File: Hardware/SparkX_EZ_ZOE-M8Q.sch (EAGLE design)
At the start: 41 parts, among them J4 U.FL, Q2 20V/4.2A/52mΩ/1.4W, U1 UBLOX_ZOE_M8-0-10, X1 32.768kHz

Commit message: Review updates
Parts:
- U1: value UBLOX_ZOE_M8-0-10 -> U-BLOX_ZOE_M8Q-0-10; device SparkFun-GPS:UBLOX_ZOE_M8-0-10 -> SparkFun-GPS:U-BLOX_ZOE_M8Q-0-10
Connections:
- net V_BATT renamed PROC_PWR_EN
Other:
- moved on the sheet: C10, C11, L1, RXD, TXD, X1, ~{SAFEBOOT}

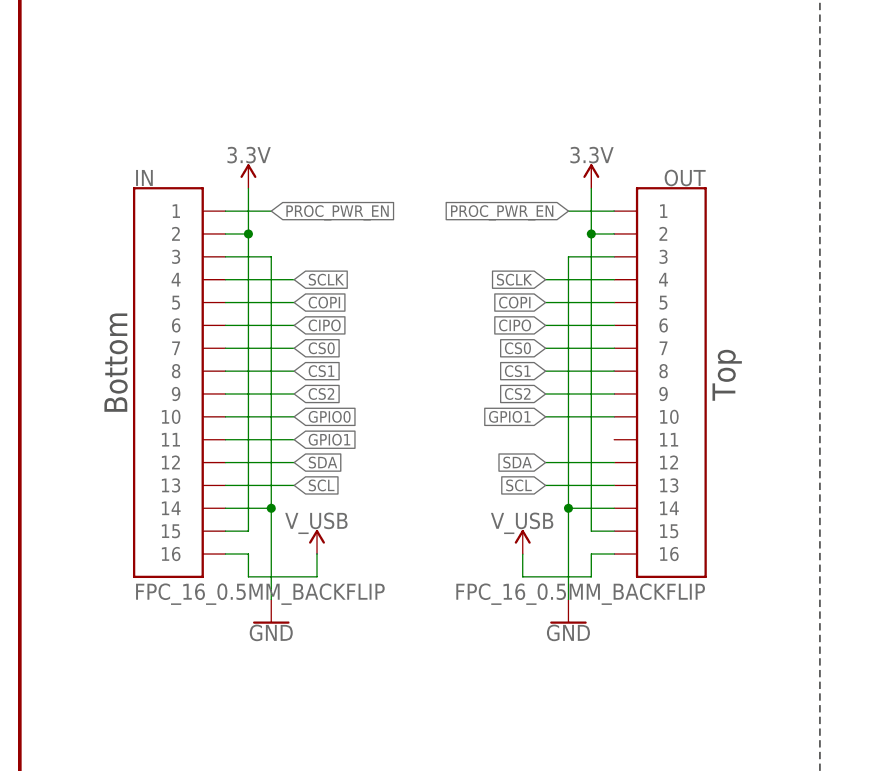
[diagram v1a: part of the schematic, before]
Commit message: Update 16-way FPC Connector
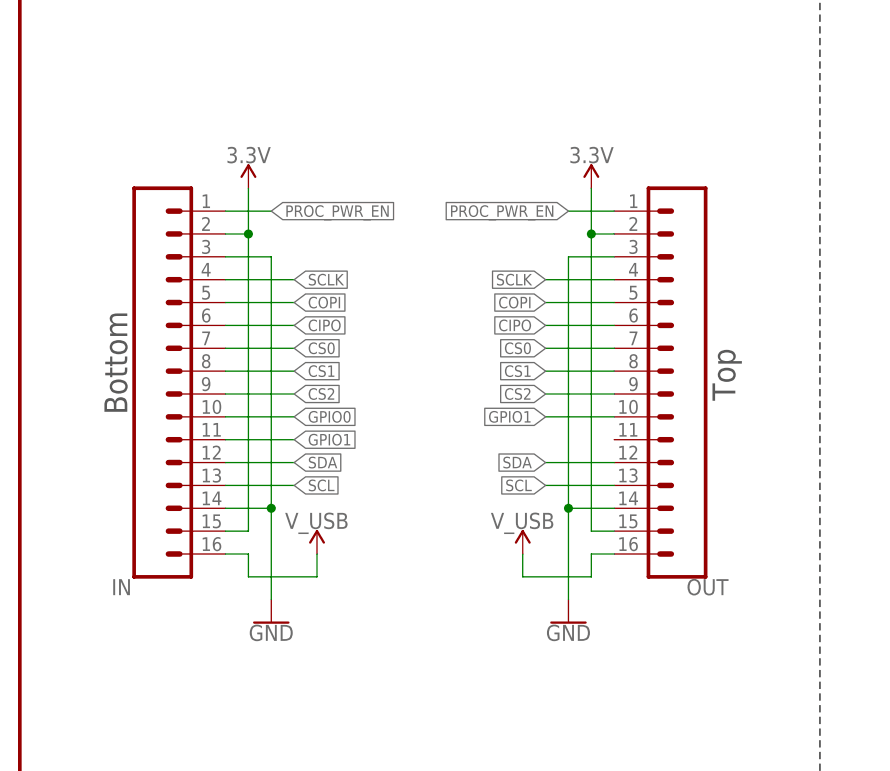
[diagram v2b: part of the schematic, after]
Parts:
- IN, OUT: value FPC_16_0.5MM_BACKFLIP -> (none); device New_Parts_Connectors:FPC_16_0.5MM_BACKFLIP -> SparkFun-Connectors:CONN_16FPC_16_0.5MM
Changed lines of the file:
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@@
 <part name="GND14" library="SparkFun-PowerSymbols" deviceset="GND" device=""/>
 <part name="SUPPLY4" library="SparkFun-PowerSymbols" deviceset="VDD" device=""/>
-<part name="IN" library="New_Parts_Connectors" deviceset="FPC_16_0.5MM" device="_BACKFLIP"/>
-<part name="OUT" library="New_Parts_Connectors" deviceset="FPC_16_0.5MM" device="_BACKFLIP"/>
+<part name="IN" library="SparkFun-Connectors" deviceset="CONN_16" device="FPC_16_0.5MM"/>
+<part name="OUT" library="SparkFun-Connectors" deviceset="CONN_16" device="FPC_16_0.5MM"/>
 <part name="SUPPLY21" library="SparkFun-PowerSymbols" deviceset="3.3V" device=""/>
 <part name="SUPPLY22" library="SparkFun-PowerSymbols" deviceset="3.3V" device=""/>
@@
 <instance part="LOGO3" gate="G$1" x="307.34" y="25.4" smashed="yes"/>
 <instance part="U$4" gate="G$1" x="307.34" y="7.62" smashed="yes"/>
-<instance part="IN" gate="G$1" x="15.24" y="45.72" smashed="yes">
-<attribute name="NAME" x="12.7" y="66.294" size="1.778" layer="95"/>
-<attribute name="VALUE" x="12.7" y="20.32" size="1.778" layer="96"/>
-</instance>
-<instance part="OUT" gate="G$1" x="73.66" y="45.72" smashed="yes" rot="MR0">
-<attribute name="NAME" x="76.2" y="66.294" size="1.778" layer="95" rot="MR0"/>
-<attribute name="VALUE" x="76.2" y="20.32" size="1.778" layer="96" rot="MR0"/>
+<instance part="IN" gate="G$1" x="12.7" y="43.18" smashed="yes" rot="MR180">
+<attribute name="NAME" x="10.16" y="22.606" size="1.778" layer="95" rot="MR180"/>
+<attribute name="VALUE" x="10.16" y="68.58" size="1.778" layer="96" rot="MR180"/>
+</instance>
+<instance part="OUT" gate="G$1" x="76.2" y="43.18" smashed="yes" rot="R180">
+<attribute name="NAME" x="78.74" y="22.606" size="1.778" layer="95" rot="R180"/>
+<attribute name="VALUE" x="78.74" y="68.58" size="1.778" layer="96" rot="R180"/>
 </instance>
 <instance part="SUPPLY21" gate="G$1" x="25.4" y="66.04" smashed="yes">
@@
 <segment>
 <pinref part="SUPPLY21" gate="G$1" pin="3.3V"/>
-<wire x1="25.4" y1="66.04" x2="25.4" y2="60.96" width="0.1524" layer="91"/>
 <pinref part="IN" gate="G$1" pin="2"/>
-<wire x1="25.4" y1="60.96" x2="22.86" y2="60.96" width="0.1524" layer="91"/>
 <pinref part="IN" gate="G$1" pin="15"/>
 <wire x1="22.86" y1="27.94" x2="25.4" y2="27.94" width="0.1524" layer="91"/>
 <wire x1="25.4" y1="27.94" x2="25.4" y2="60.96" width="0.1524" layer="91"/>
+<wire x1="25.4" y1="60.96" x2="25.4" y2="66.04" width="0.1524" layer="91"/>
+<wire x1="22.86" y1="60.96" x2="25.4" y2="60.96" width="0.1524" layer="91"/>
 <junction x="25.4" y="60.96"/>
 </segment>
 <segment>
 <pinref part="SUPPLY22" gate="G$1" pin="3.3V"/>
-<wire x1="63.5" y1="66.04" x2="63.5" y2="60.96" width="0.1524" layer="91"/>
 <pinref part="OUT" gate="G$1" pin="2"/>
-<wire x1="63.5" y1="60.96" x2="66.04" y2="60.96" width="0.1524" layer="91"/>
 <pinref part="OUT" gate="G$1" pin="15"/>
 <wire x1="66.04" y1="27.94" x2="63.5" y2="27.94" width="0.1524" layer="91"/>
 <wire x1="63.5" y1="27.94" x2="63.5" y2="60.96" width="0.1524" layer="91"/>
+<wire x1="63.5" y1="60.96" x2="63.5" y2="66.04" width="0.1524" layer="91"/>
+<wire x1="66.04" y1="60.96" x2="63.5" y2="60.96" width="0.1524" layer="91"/>
 <junction x="63.5" y="60.96"/>
 </segment>
@@
 <pinref part="IN" gate="G$1" pin="16"/>
 <wire x1="22.86" y1="25.4" x2="25.4" y2="25.4" width="0.1524" layer="91"/>
-<wire x1="25.4" y1="22.86" x2="25.4" y2="25.4" width="0.1524" layer="91"/>
-</segment>
-<segment>
+<wire x1="25.4" y1="25.4" x2="25.4" y2="22.86" width="0.1524" layer="91"/>
+</segment>
+<segment>
